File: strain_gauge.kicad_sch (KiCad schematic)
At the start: 6 parts, among them U4 INA826

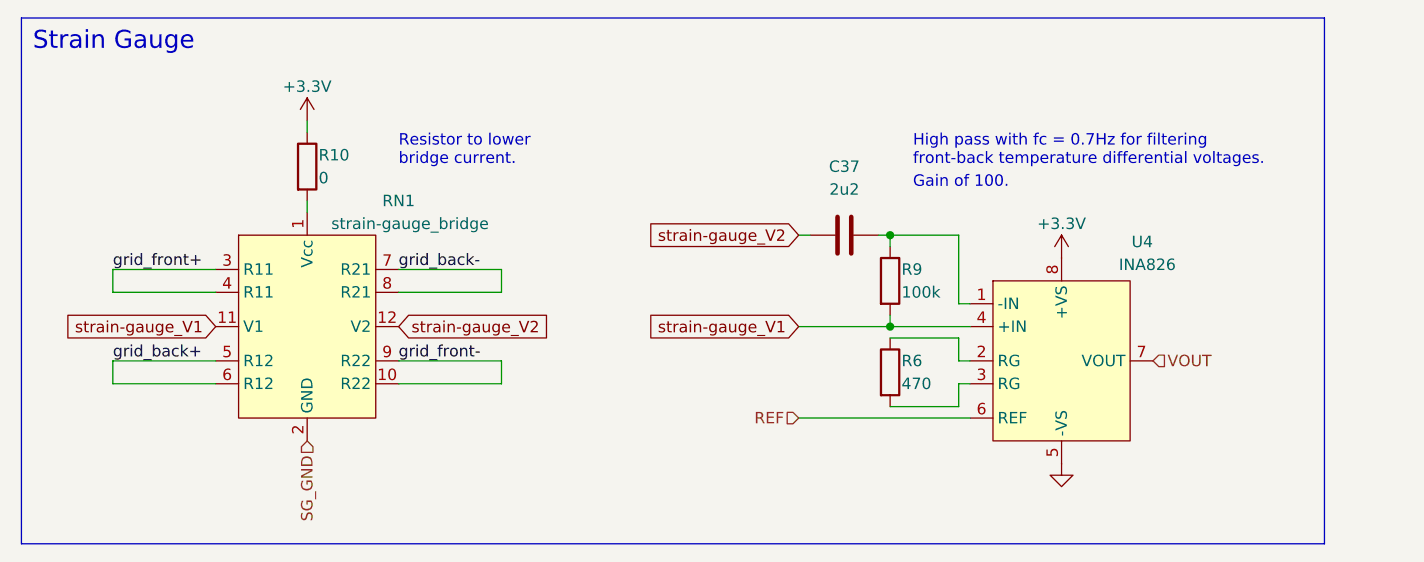
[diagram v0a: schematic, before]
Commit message: 3.3V and 5V power supply tweaks
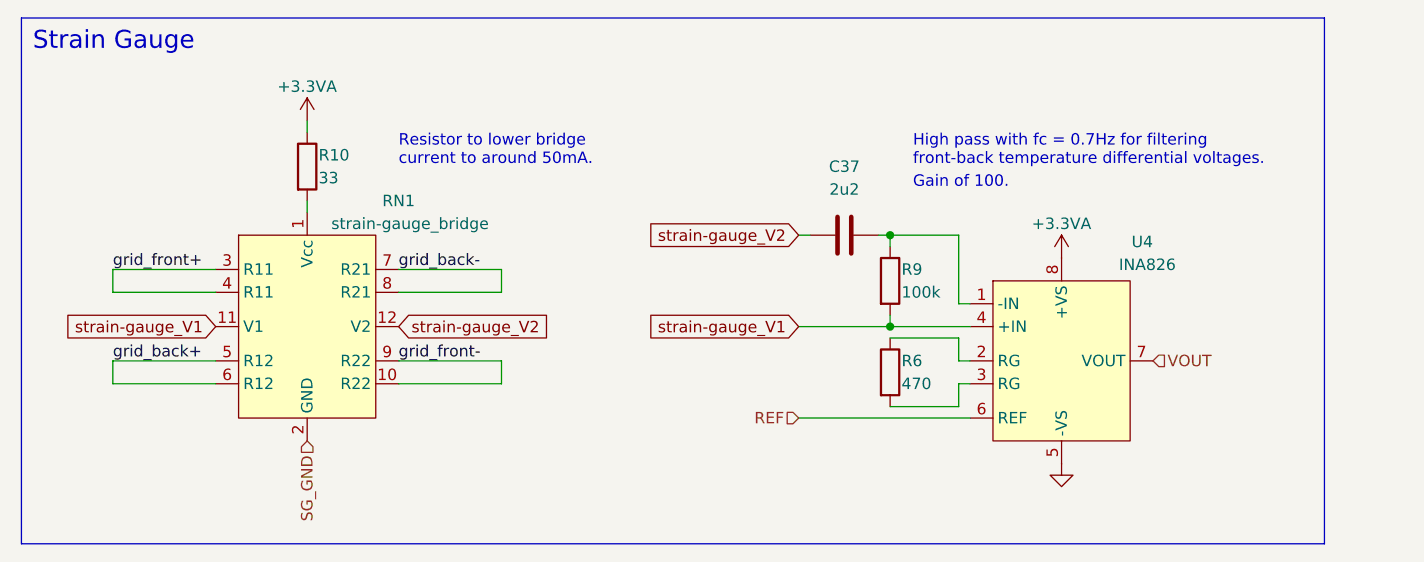
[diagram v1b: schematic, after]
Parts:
- R10: value 0 -> 33
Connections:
- net +3.3V renamed +3.3VA
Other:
- note added: "Resistor to lower bridge current to around 50mA."
- note removed: "Resistor to lower bridge current."
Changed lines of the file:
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@@
     (fill (type none))
   )
-  (text "Resistor to lower\nbridge current." (at 55.88 30.48 0)
+  (text "Resistor to lower bridge\ncurrent to around 50mA." (at 55.88 30.48 0)
     (effects (font (size 1.27 1.27)) (justify left bottom))
   )
@@
     )
   )
+  (symbol (lib_id "power:+3.3VA") (at 45.72 25.4 0) (unit 1)
+    (in_bom yes) (on_board yes) (dnp no)
+    (property "Reference" "#PWR012" (at 45.72 29.21 0)
+      (effects (font (size 1.27 1.27)) hide)
+    )
+    (property "Value" "+3.3VA" (at 45.72 21.59 0)
+      (effects (font (size 1.27 1.27)))
+    )
+    (property "Footprint" "" (at 45.72 25.4 0)
+      (effects (font (size 1.27 1.27)) hide)
+    )
+    (property "Datasheet" "" (at 45.72 25.4 0)
+      (effects (font (size 1.27 1.27)) hide)
+    )
+    (pin "1")
+    (instances
+      (project "frodo_fancyfins"
+        (path "/6b822b14-450b-45c3-a34b-8e18c5811754"
+          (reference "#PWR012") (unit 1)
+        )
+        (path "/6b822b14-450b-45c3-a34b-8e18c5811754/49cec511-7b13-4cbc-87f1-b842fd9f9998"
+          (reference "#PWR068") (unit 1)
+        )
+        (path "/6b822b14-450b-45c3-a34b-8e18c5811754/5195ebe2-c291-4ed3-9cd9-cf447ee2c8e4"
+          (reference "#PWR069") (unit 1)
+        )
+      )
+    )
+  )
   (symbol (lib_id "power:GND") (at 129.54 63.5 0) (unit 1)
     (in_bom yes) (on_board yes) (dnp no) (fields_autoplaced)
@@
     )
   )
-  (symbol (lib_id "power:+3.3V") (at 129.54 40.64 0) (unit 1)
-    (in_bom yes) (on_board yes) (dnp no)
-    (property "Reference" "#PWR067" (at 129.54 44.45 0)
-      (effects (font (size 1.27 1.27)) hide)
-    )
-    (property "Value" "+3.3V" (at 129.54 36.83 0)
-      (effects (font (size 1.27 1.27)))
-    )
-    (property "Footprint" "" (at 129.54 40.64 0)
-      (effects (font (size 1.27 1.27)) hide)
-    )
-    (property "Datasheet" "" (at 129.54 40.64 0)
-      (effects (font (size 1.27 1.27)) hide)
-    )
-    (pin "1")
-    (instances
-      (project "frodo_fancyfins"
-        (path "/6b822b14-450b-45c3-a34b-8e18c5811754/49cec511-7b13-4cbc-87f1-b842fd9f9998"
-          (reference "#PWR067") (unit 1)
-        )
-        (path "/6b822b14-450b-45c3-a34b-8e18c5811754/5195ebe2-c291-4ed3-9cd9-cf447ee2c8e4"
-          (reference "#PWR070") (unit 1)
-        )
-      )
-    )
-  )
-  (symbol (lib_id "power:+3.3V") (at 45.72 25.4 0) (unit 1)
-    (in_bom yes) (on_board yes) (dnp no)
-    (property "Reference" "#PWR068" (at 45.72 29.21 0)
-      (effects (font (size 1.27 1.27)) hide)
-    )
-    (property "Value" "+3.3V" (at 45.72 21.59 0)
-      (effects (font (size 1.27 1.27)))
-    )
-    (property "Footprint" "" (at 45.72 25.4 0)
-      (effects (font (size 1.27 1.27)) hide)
-    )
-    (property "Datasheet" "" (at 45.72 25.4 0)
-      (effects (font (size 1.27 1.27)) hide)
-    )
-    (pin "1")
-    (instances
-      (project "frodo_fancyfins"
-        (path "/6b822b14-450b-45c3-a34b-8e18c5811754/49cec511-7b13-4cbc-87f1-b842fd9f9998"
-          (reference "#PWR068") (unit 1)
-        )
-        (path "/6b822b14-450b-45c3-a34b-8e18c5811754/5195ebe2-c291-4ed3-9cd9-cf447ee2c8e4"
-          (reference "#PWR069") (unit 1)
-        )
-      )
-    )
-  )
   (symbol (lib_id "Device:R") (at 110.49 53.34 0) (unit 1)
     (in_bom yes) (on_board yes) (dnp no)
@@
       (effects (font (size 1.27 1.27)) (justify left))
     )
-    (property "Value" "0" (at 46.99 31.75 0)
+    (property "Value" "33" (at 46.99 31.75 0)
       (effects (font (size 1.27 1.27)) (justify left))
     )
@@
         )
       )
+    )
+  )
+  (symbol (lib_id "power:+3.3VA") (at 129.54 40.64 0) (unit 1)
+    (in_bom yes) (on_board yes) (dnp no)
+    (property "Reference" "#PWR012" (at 129.54 44.45 0)
+      (effects (font (size 1.27 1.27)) hide)
+    )
+    (property "Value" "+3.3VA" (at 129.54 36.83 0)
+      (effects (font (size 1.27 1.27)))
+    )
+    (property "Footprint" "" (at 129.54 40.64 0)
+      (effects (font (size 1.27 1.27)) hide)
+    )
+    (property "Datasheet" "" (at 129.54 40.64 0)
+      (effects (font (size 1.27 1.27)) hide)
+    )
+    (pin "1")
+    (instances
+      (project "frodo_fancyfins"
+        (path "/6b822b14-450b-45c3-a34b-8e18c5811754"
+          (reference "#PWR012") (unit 1)
+        )
+        (path "/6b822b14-450b-45c3-a34b-8e18c5811754/49cec511-7b13-4cbc-87f1-b842fd9f9998"
+          (reference "#PWR067") (unit 1)
+        )
+        (path "/6b822b14-450b-45c3-a34b-8e18c5811754/5195ebe2-c291-4ed3-9cd9-cf447ee2c8e4"
+          (reference "#PWR070") (unit 1)
+        )
+      )

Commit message: Asign footprints, add missing footprints, adjust Rext.
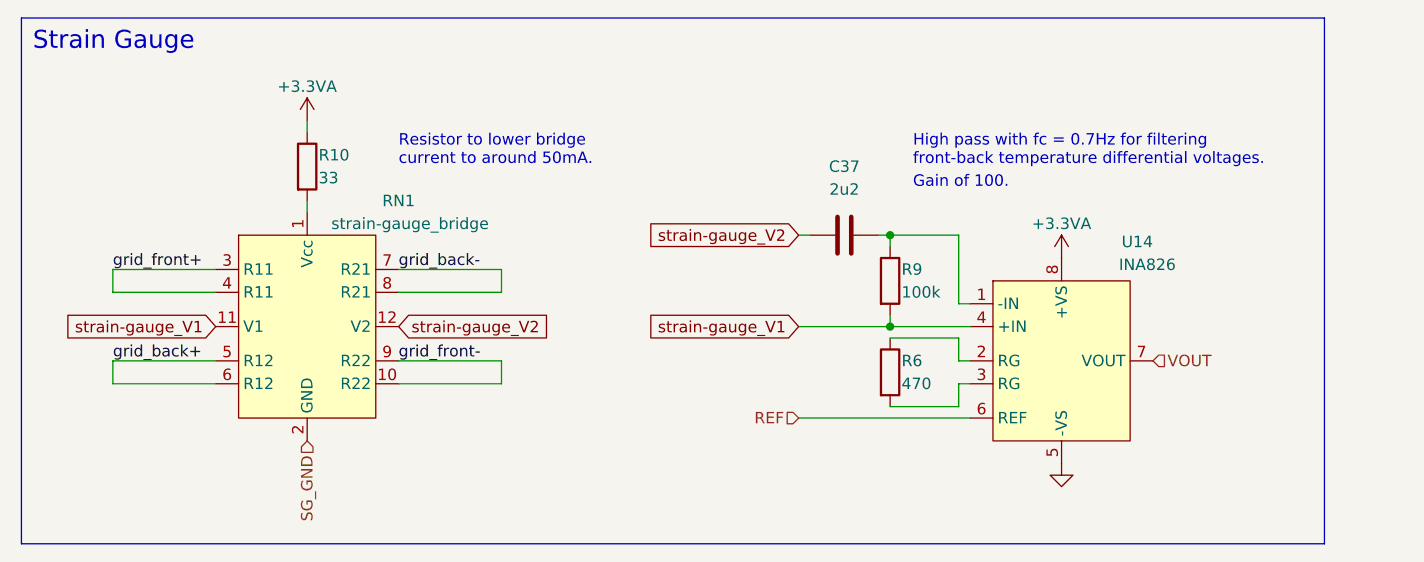
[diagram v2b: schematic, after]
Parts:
- removed U4: INA826, symbol frodo_fancyfins:INA826
- added U14: INA826, Package_SO:SOIC-8-1EP_3.9x4.9mm_P1.27mm_EP2.29x3mm, symbol frodo_fancyfins:INA826
- C37: footprint (none) -> Capacitor_SMD:C_0603_1608Metric_Pad1.08x0.95mm_HandSolder
- R10, R6, R9: footprint (none) -> Resistor_SMD:R_0402_1005Metric_Pad0.72x0.64mm_HandSolder
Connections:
- net +3.3VA: now also U14.8 (+VS)
- net GND: now also U14.5 (-VS)
- net REF: now also U14.6 (REF)
- net VOUT: now also U14.7 (VOUT)
- net strain-gauge_V1: now also U14.4 (+IN)
- net at C37.2, R9.1: now also U14.1 (-IN)
- net at R6.1: now also U14.2 (RG)
- net at R6.2: now also U14.3 (RG)
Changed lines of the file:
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@@
     (effects (font (size 1.27 1.27)) (justify left))
-  )
-  (symbol (lib_id "frodo_fancyfins:INA826") (at 129.54 52.07 0) (unit 1)
-    (in_bom yes) (on_board yes) (dnp no) (fields_autoplaced)
-    (property "Reference" "U4" (at 139.7 38.1 0) (do_not_autoplace)
-      (effects (font (size 1.27 1.27)) (justify right top))
-    )
-    (property "Value" "INA826" (at 142.24 40.64 0) (do_not_autoplace)
-      (effects (font (size 1.27 1.27)) (justify right top))
-    )
-    (property "Footprint" "" (at 148.59 29.21 0)
-      (effects (font (size 1.27 1.27)) hide)
-    )
-    (property "Datasheet" "" (at 148.59 29.21 0)
-      (effects (font (size 1.27 1.27)) hide)
-    )
-    (pin "8")
-    (pin "7")
-    (pin "6")
-    (pin "5")
-    (pin "3")
-    (pin "4")
-    (pin "2")
-    (pin "1")
-    (instances
-      (project "frodo_fancyfins"
-        (path "/6b822b14-450b-45c3-a34b-8e18c5811754/49cec511-7b13-4cbc-87f1-b842fd9f9998"
-          (reference "U4") (unit 1)
-        )
-        (path "/6b822b14-450b-45c3-a34b-8e18c5811754/5195ebe2-c291-4ed3-9cd9-cf447ee2c8e4"
-          (reference "U13") (unit 1)
-        )
-      )
-    )
   )
   (symbol (lib_id "power:+3.3VA") (at 45.72 25.4 0) (unit 1)
@@
       (effects (font (size 1.27 1.27)) (justify left))
     )
-    (property "Footprint" "" (at 108.712 43.18 90)
+    (property "Footprint" "Resistor_SMD:R_0402_1005Metric_Pad0.72x0.64mm_HandSolder" (at 108.712 43.18 90)
       (effects (font (size 1.27 1.27)) hide)
     )
@@
       (effects (font (size 1.27 1.27)) (justify left))
     )
-    (property "Footprint" "" (at 108.712 53.34 90)
+    (property "Footprint" "Resistor_SMD:R_0402_1005Metric_Pad0.72x0.64mm_HandSolder" (at 108.712 53.34 90)
       (effects (font (size 1.27 1.27)) hide)
     )
@@
     )
   )
+  (symbol (lib_name "INA826_1") (lib_id "frodo_fancyfins:INA826") (at 129.54 52.07 0) (unit 1)
+    (in_bom yes) (on_board yes) (dnp no) (fields_autoplaced)
+    (property "Reference" "U14" (at 139.7 38.1 0) (do_not_autoplace)
+      (effects (font (size 1.27 1.27)) (justify right top))
+    )
+    (property "Value" "INA826" (at 142.24 40.64 0) (do_not_autoplace)
+      (effects (font (size 1.27 1.27)) (justify right top))
+    )
+    (property "Footprint" "Package_SO:SOIC-8-1EP_3.9x4.9mm_P1.27mm_EP2.29x3mm" (at 148.59 29.21 0)
+      (effects (font (size 1.27 1.27)) hide)
+    )
+    (property "Datasheet" "" (at 148.59 29.21 0)
+      (effects (font (size 1.27 1.27)) hide)
+    )
+    (pin "1")
+    (pin "6")
+    (pin "2")
+    (pin "4")
+    (pin "7")
+    (pin "5")
+    (pin "8")
+    (pin "3")
+    (instances
+      (project "frodo_fancyfins"
+        (path "/6b822b14-450b-45c3-a34b-8e18c5811754/49cec511-7b13-4cbc-87f1-b842fd9f9998"
+          (reference "U14") (unit 1)
+        )
+        (path "/6b822b14-450b-45c3-a34b-8e18c5811754/5195ebe2-c291-4ed3-9cd9-cf447ee2c8e4"
+          (reference "U19") (unit 1)
+        )
+      )
+    )
+  )
   (symbol (lib_id "Device:R") (at 45.72 30.48 0) (unit 1)
     (in_bom yes) (on_board yes) (dnp no)
@@
       (effects (font (size 1.27 1.27)) (justify left))
     )
-    (property "Footprint" "" (at 43.942 30.48 90)
+    (property "Footprint" "Resistor_SMD:R_0402_1005Metric_Pad0.72x0.64mm_HandSolder" (at 43.942 30.48 90)
       (effects (font (size 1.27 1.27)) hide)
     )
@@
       (effects (font (size 1.27 1.27)))
     )
-    (property "Footprint" "" (at 109.22 37.1348 0)
+    (property "Footprint" "Capacitor_SMD:C_0603_1608Metric_Pad1.08x0.95mm_HandSolder" (at 109.22 37.1348 0)
       (effects (font (size 1.27 1.27)) hide)
     )
